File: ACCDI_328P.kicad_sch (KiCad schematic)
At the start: 44 parts, among them IC1 MJE340G, J1 Conn_01x05_Female, Q1 2N2222, Q2 2N2222, U1 LR8N3-G, U2 ATmega328P-P

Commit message: 2 layer board
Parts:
- added H7: Kill Switch, MountingHole:MountingHole_2.2mm_M2_Pad_TopBottom, symbol Mechanical:MountingHole_Pad
- R3: footprint Resistor_THT:R_Axial_DIN0516_L15.5mm_D5.0mm_P30.48mm_Horizontal -> Resistor_THT:R_Axial_DIN0516_L15.5mm_D5.0mm_P20.32mm_Horizontal
- Y1: renamed from Y?; footprint HC49S1630507030ATF -> Crystal:Resonator-2Pin_W10.0mm_H5.0mm
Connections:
- net at D8.1 (K), H5.1, R9.1: now also H7.1
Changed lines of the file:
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@@
+    (stroke (width 0) (type default) (color 0 0 0 0))
+  )
+  (wire (pts (xy 270.51 52.07) (xy 270.51 60.96))
     (stroke (width 0) (type default) (color 0 0 0 0))
   )
@@
   )
   (wire (pts (xy 219.71 60.96) (xy 219.71 66.04))
+    (stroke (width 0) (type default) (color 0 0 0 0))
+  )
+  (wire (pts (xy 276.86 52.07) (xy 270.51 52.07))
     (stroke (width 0) (type default) (color 0 0 0 0))
   )
@@
       (effects (font (size 1.27 1.27)) (justify left))
     )
-    (property "Footprint" "Resistor_THT:R_Axial_DIN0516_L15.5mm_D5.0mm_P30.48mm_Horizontal" (id 2) (at 94.742 43.18 90)
+    (property "Footprint" "Resistor_THT:R_Axial_DIN0516_L15.5mm_D5.0mm_P20.32mm_Horizontal" (id 2) (at 94.742 43.18 90)
       (effects (font (size 1.27 1.27)) hide)
     )
@@
   (symbol (lib_id "HC49S-16-30-50-70-30-ATF:HC49S-16-30-50-70-30-ATF") (at 189.23 114.3 90) (unit 1)
     (in_bom yes) (on_board yes)
-    (property "Reference" "Y?" (id 0) (at 194.31 107.9499 90)
+    (property "Reference" "Y1" (id 0) (at 194.31 107.9499 90)
       (effects (font (size 1.27 1.27)) (justify right))
     )
@@
       (effects (font (size 1.27 1.27)) (justify right))
     )
-    (property "Footprint" "HC49S1630507030ATF" (id 2) (at 187.96 105.41 0)
+    (property "Footprint" "Crystal:Resonator-2Pin_W10.0mm_H5.0mm" (id 2) (at 187.96 105.41 0)
       (effects (font (size 1.27 1.27)) (justify left) hide)
     )
@@
     )
     (property "Datasheet" "~" (id 3) (at 20.32 34.29 0)
+      (effects (font (size 1.27 1.27)) hide)
+    )
+    (pin "1")
+  )
+  (symbol (lib_id "Mechanical:MountingHole_Pad") (at 279.4 52.07 270) (unit 1)
+    (in_bom yes) (on_board yes)
+    (property "Reference" "H7" (id 0) (at 276.86 45.72 90)
+      (effects (font (size 1.27 1.27)) (justify right))
+    )
+    (property "Value" "Kill Switch" (id 1) (at 298.45 52.07 90)
+      (effects (font (size 1.27 1.27)) (justify right))
+    )
+    (property "Footprint" "MountingHole:MountingHole_2.2mm_M2_Pad_TopBottom" (id 2) (at 279.4 52.07 0)
+      (effects (font (size 1.27 1.27)) hide)
+    )
+    (property "Datasheet" "~" (id 3) (at 279.4 52.07 0)
       (effects (font (size 1.27 1.27)) hide)
     )
@@
       (reference "H6") (unit 1) (value "Pickup Coil -") (footprint "MountingHole:MountingHole_2.2mm_M2_Pad_TopBottom")
     )
+    (path "/4264f49a-4e24-4d74-9ebc-416cda027254"
+      (reference "H7") (unit 1) (value "Kill Switch") (footprint "MountingHole:MountingHole_2.2mm_M2_Pad_TopBottom")
+    )
     (path "/defeb2d8-e81a-499d-9596-7e93c840ae7b"
       (reference "IC1") (unit 1) (value "MJE340G") (footprint "TO229P300X760X1364-3P")
@@
     )
     (path "/10915874-20b6-4b78-8c92-95e5eaf9576c"
-      (reference "R3") (unit 1) (value "27 1 watt") (footprint "Resistor_THT:R_Axial_DIN0516_L15.5mm_D5.0mm_P30.48mm_Horizontal")
+      (reference "R3") (unit 1) (value "27 1 watt") (footprint "Resistor_THT:R_Axial_DIN0516_L15.5mm_D5.0mm_P20.32mm_Horizontal")
     )
     (path "/0e76ecea-e2c2-4087-a6f7-96033bef8143"
@@
     )
     (path "/2ff737f8-83ff-4edb-ba19-df92d673e931"
-      (reference "Y?") (unit 1) (value "HC49S-16-30-50-70-30-ATF") (footprint "HC49S1630507030ATF")
-    )
-  )
+      (reference "Y1") (unit 1) (value "HC49S-16-30-50-70-30-ATF") (footprint "Crystal:Resonator-2Pin_W10.0mm_H5.0mm")
+    )
+  )

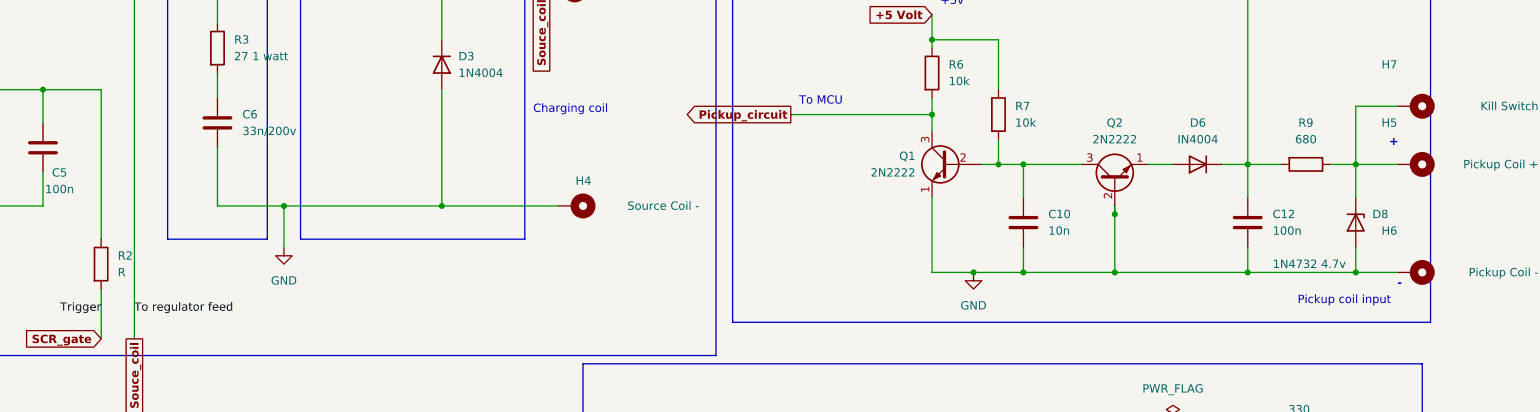
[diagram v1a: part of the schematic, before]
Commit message: Removed zenner diode
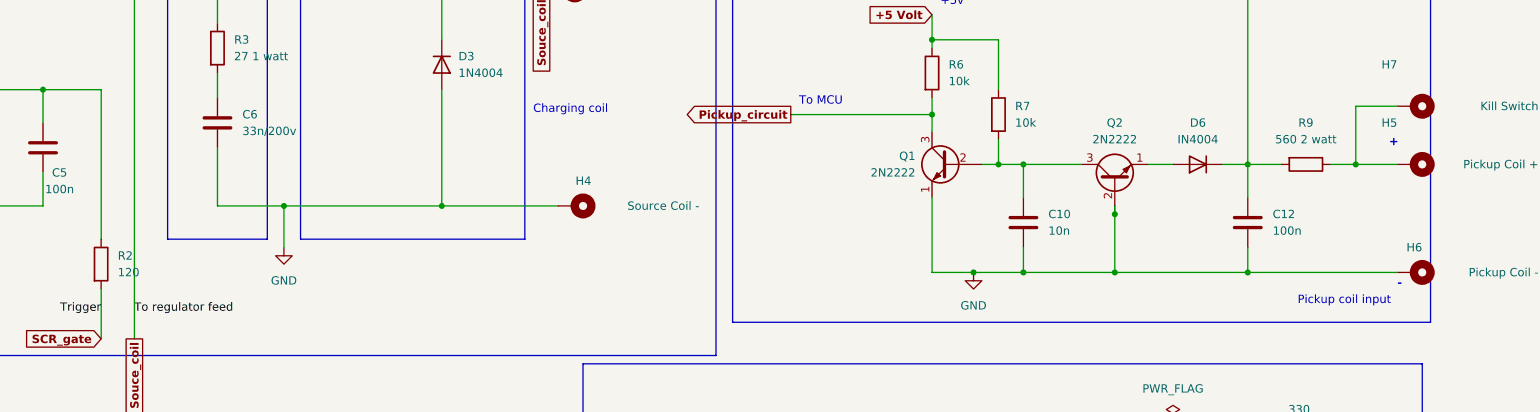
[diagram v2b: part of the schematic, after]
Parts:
- removed D8: 1N4732 4.7v, Diode_THT:D_DO-41_SOD81_P10.16mm_Horizontal, symbol Diode:1N47xxA
- R2: value R -> 120
- R9: value 680 -> 560 2 watt
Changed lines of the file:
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@@
   (junction (at 233.68 68.58) (diameter 0) (color 0 0 0 0)
-  )
-  (junction (at 270.51 77.47) (diameter 0) (color 0 0 0 0)
   )
   (junction (at 86.36 132.08) (diameter 0) (color 0 0 0 0)
@@
     (stroke (width 0) (type default) (color 0 0 0 0))
   )
-  (wire (pts (xy 254 77.47) (xy 270.51 77.47))
-    (stroke (width 0) (type default) (color 0 0 0 0))
-  )
   (wire (pts (xy 205.74 77.47) (xy 212.09 77.47))
     (stroke (width 0) (type default) (color 0 0 0 0))
@@
     (stroke (width 0) (type default) (color 0 0 0 0))
   )
-  (wire (pts (xy 270.51 73.66) (xy 270.51 77.47))
-    (stroke (width 0) (type default) (color 0 0 0 0))
-  )
   (wire (pts (xy 100.33 139.7) (xy 100.33 144.78))
     (stroke (width 0) (type default) (color 0 0 0 0))
@@
     (stroke (width 0) (type default) (color 0 0 0 0))
   )
-  (wire (pts (xy 270.51 77.47) (xy 276.86 77.47))
+  (wire (pts (xy 254 77.47) (xy 276.86 77.47))
     (stroke (width 0) (type default) (color 0 0 0 0))
   )
@@
   )
   (polyline (pts (xy 137.16 102.87) (xy 137.16 182.88))
-    (stroke (width 0) (type default) (color 0 0 0 0))
-  )
-  (wire (pts (xy 270.51 60.96) (xy 270.51 66.04))
     (stroke (width 0) (type default) (color 0 0 0 0))
   )
@@
       (effects (font (size 1.27 1.27)) (justify left))
     )
-    (property "Value" "R" (id 1) (at 81.28 77.4699 0)
+    (property "Value" "120" (id 1) (at 81.28 77.4699 0)
       (effects (font (size 1.27 1.27)) (justify left))
     )
@@
   (symbol (lib_id "Mechanical:MountingHole_Pad") (at 279.4 77.47 270) (unit 1)
     (in_bom yes) (on_board yes)
-    (property "Reference" "H6" (id 0) (at 276.86 71.12 90)
+    (property "Reference" "H6" (id 0) (at 280.67 73.66 90)
       (effects (font (size 1.27 1.27)) (justify right))
     )
@@
     (in_bom yes) (on_board yes) (fields_autoplaced)
     (property "Reference" "R9" (id 0) (at 262.89 54.61 90))
-    (property "Value" "680" (id 1) (at 262.89 57.15 90))
+    (property "Value" "560 2 watt" (id 1) (at 262.89 57.15 90))
     (property "Footprint" "Resistor_THT:R_Axial_DIN0309_L9.0mm_D3.2mm_P12.70mm_Horizontal" (id 2) (at 262.89 59.182 90)
       (effects (font (size 1.27 1.27)) hide)
@@
     (pin "9")
   )
-  (symbol (lib_id "Diode:1N47xxA") (at 270.51 69.85 270) (unit 1)
-    (in_bom yes) (on_board yes)
-    (property "Reference" "D8" (id 0) (at 273.05 68.5799 90)
-      (effects (font (size 1.27 1.27)) (justify left))
-    )
-    (property "Value" "1N4732 4.7v" (id 1) (at 257.81 76.2 90)
-      (effects (font (size 1.27 1.27)) (justify left))
-    )
-    (property "Footprint" "Diode_THT:D_DO-41_SOD81_P10.16mm_Horizontal" (id 2) (at 266.065 69.85 0)
-      (effects (font (size 1.27 1.27)) hide)
-    )
-    (property "Datasheet" "https://www.vishay.com/docs/85816/1n4728a.pdf" (id 3) (at 270.51 69.85 0)
-      (effects (font (size 1.27 1.27)) hide)
-    )
-    (pin "1")
-    (pin "2")
-  )
   (symbol (lib_id "Device:D") (at 72.39 123.19 270) (unit 1)
     (in_bom yes) (on_board yes) (fields_autoplaced)
@@
       (reference "D7") (unit 1) (value "LED") (footprint "LED_THT:LED_D3.0mm")
     )
-    (path "/cdb2feb1-e36a-4973-baaa-84f7165b6c90"
-      (reference "D8") (unit 1) (value "1N4732 4.7v") (footprint "Diode_THT:D_DO-41_SOD81_P10.16mm_Horizontal")
-    )
     (path "/e93d7c27-cde1-4be9-8dad-bc9c49083a74"
       (reference "D9") (unit 1) (value "BT151-800R,127") (footprint "KiCad:TO254P470X1000X2000-3P")
@@
     )
     (path "/3084b209-f778-40a1-9f38-6314945bc7f7"
-      (reference "R2") (unit 1) (value "R") (footprint "Resistor_THT:R_Axial_DIN0309_L9.0mm_D3.2mm_P12.70mm_Horizontal")
+      (reference "R2") (unit 1) (value "120") (footprint "Resistor_THT:R_Axial_DIN0309_L9.0mm_D3.2mm_P12.70mm_Horizontal")
     )
     (path "/10915874-20b6-4b78-8c92-95e5eaf9576c"
@@
     )
     (path "/af829ac5-ca1c-469a-a031-0388655823c9"
-      (reference "R9") (unit 1) (value "680") (footprint "Resistor_THT:R_Axial_DIN0309_L9.0mm_D3.2mm_P12.70mm_Horizontal")
+      (reference "R9") (unit 1) (value "560 2 watt") (footprint "Resistor_THT:R_Axial_DIN0309_L9.0mm_D3.2mm_P12.70mm_Horizontal")
     )
     (path "/21ce4531-e772-4dff-8696-40d28f0f2010"

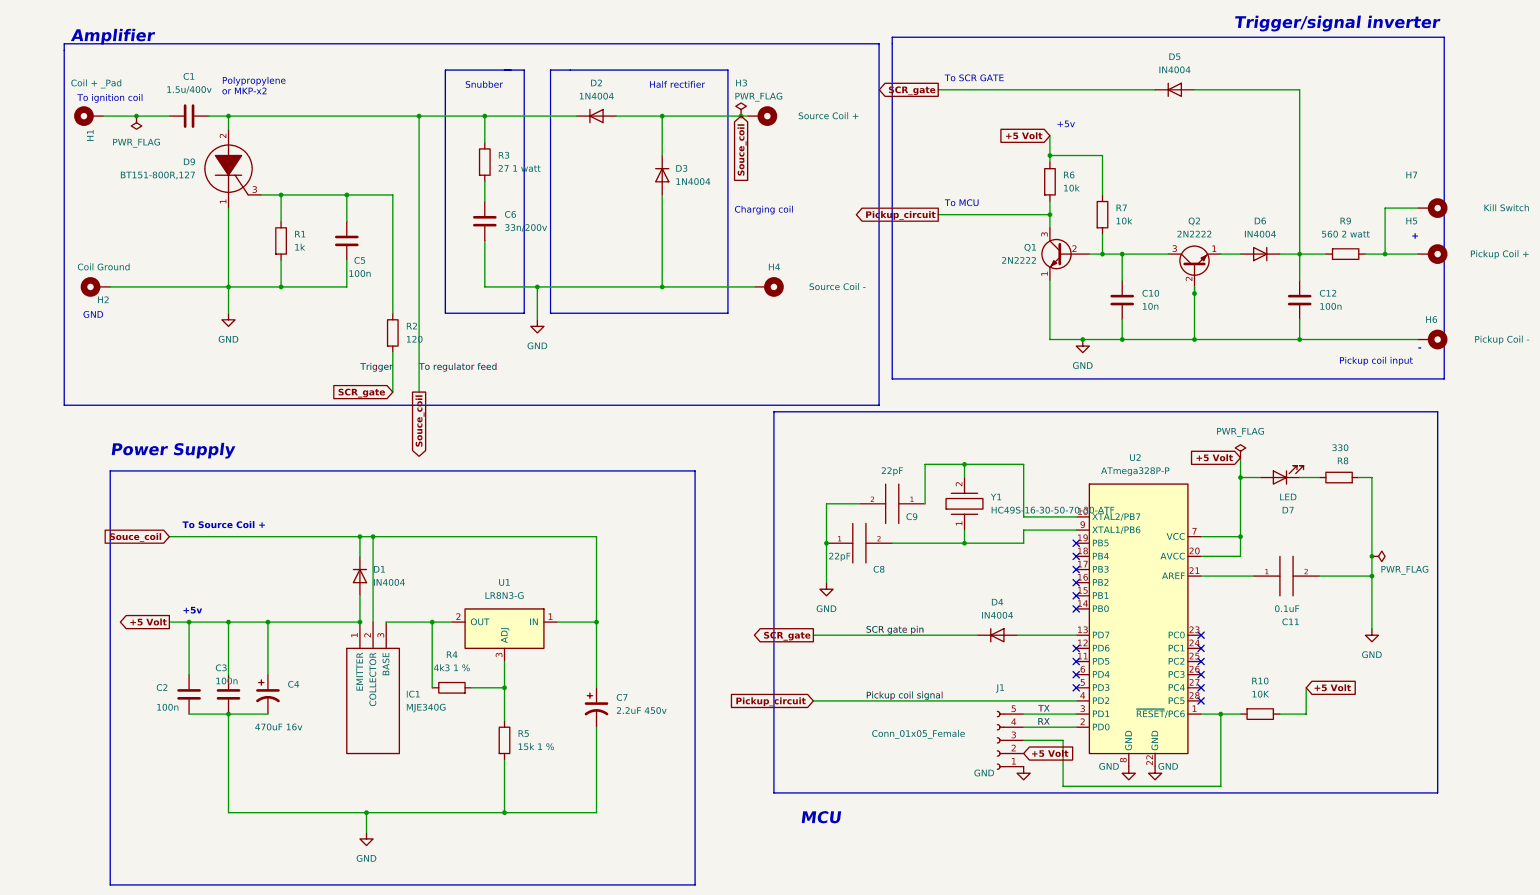
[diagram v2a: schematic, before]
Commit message: Diodes and reroute
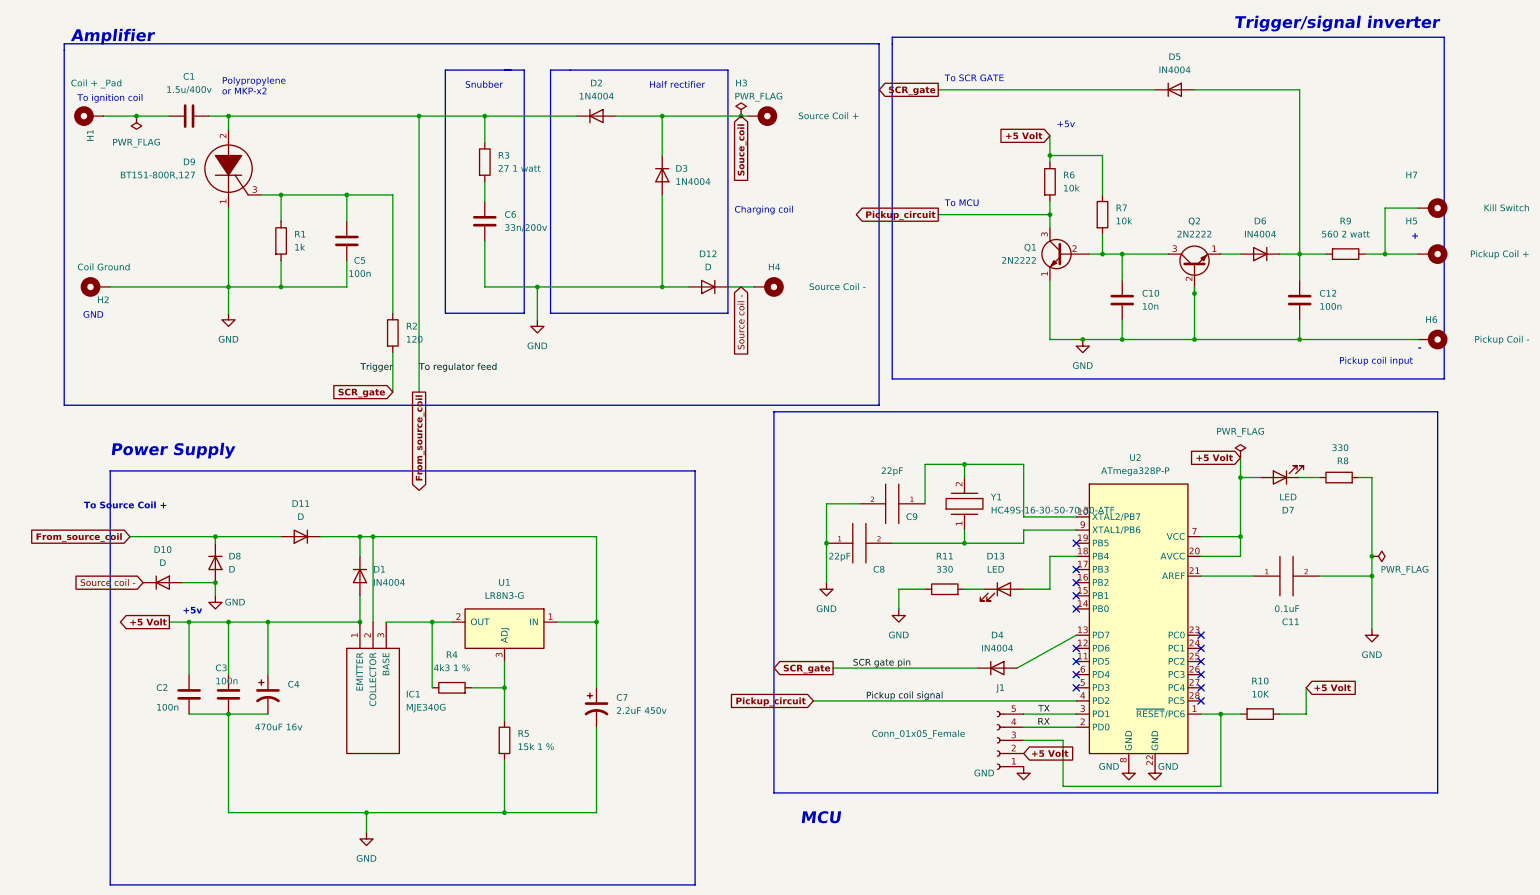
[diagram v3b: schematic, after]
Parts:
- added D10, D11, D12, D8: D, Diode_THT:D_DO-41_SOD81_P10.16mm_Horizontal, symbol Device:D
- added D13: LED, LED_THT:LED_D3.0mm, symbol Device:LED
- added R11: 330, Resistor_THT:R_Axial_DIN0309_L9.0mm_D3.2mm_P12.70mm_Horizontal, symbol Device:R
- C8, C9: footprint Capacitor_THT:C_Disc_D9.0mm_W5.0mm_P10.00mm -> Capacitor_THT:C_Disc_D5.0mm_W2.5mm_P5.00mm
- R10: footprint Resistor_THT:R_Axial_DIN0309_L9.0mm_D3.2mm_P12.70mm_Horizontal -> Resistor_THT:R_Axial_DIN0207_L6.3mm_D2.5mm_P10.16mm_Horizontal
- R9: footprint Resistor_THT:R_Axial_DIN0309_L9.0mm_D3.2mm_P12.70mm_Horizontal -> Resistor_THT:R_Axial_DIN0516_L15.5mm_D5.0mm_P20.32mm_Horizontal
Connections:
- net GND: now also D10.2 (A), D12.2 (A), D8.2 (A), R11.1; no longer H4.1
- net Souce_coil: no longer C1.1, C7.1, D1.1 (K), D2.1 (K), D9.2, IC1.2 (COLLECTOR), R3.1, U1.1 (IN)
- net at U2.18 (PB4): now also D13.2 (A)
- new net: D13.1 (K), R11.2
- new net: C7.1, D1.1 (K), D11.1 (K), IC1.2 (COLLECTOR), U1.1 (IN)
- new net From_source_coil: C1.1, D11.2 (A), D2.1 (K), D8.1 (K), D9.2, R3.1
- new net Source coil -: D10.1 (K), D12.1 (K), H4.1
- no-connect marks 16 -> 15
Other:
- moved on the sheet: D4
